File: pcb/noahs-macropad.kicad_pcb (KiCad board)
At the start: 2 copper layers, 99 x 39 mm, 17 parts, among them U1 MOUDLE-SEEEDUINO-XIAO

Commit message: moved things around, to make it look less like an offcentered brick
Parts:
- added D10: LED_SK6812MINI, ScottoKeebs_Components:LED_SK6812MINI, F.Cu at (75.0, 121.4)
- added D11: LED_SK6812MINI, ScottoKeebs_Components:LED_SK6812MINI, F.Cu at (75.0, 125.5)
- added D12: LED_SK6812MINI, ScottoKeebs_Components:LED_SK6812MINI, F.Cu at (75.0, 129.6)
- added D13: LED_SK6812MINI, ScottoKeebs_Components:LED_SK6812MINI, F.Cu at (75.0, 133.8)
- added D14: LED_SK6812MINI, ScottoKeebs_Components:LED_SK6812MINI, F.Cu at (75.0, 137.9)
- added D15: LED_SK6812MINI, ScottoKeebs_Components:LED_SK6812MINI, F.Cu at (75.0, 142.0)
- added D16: LED_SK6812MINI, ScottoKeebs_Components:LED_SK6812MINI, F.Cu at (74.9, 146.2)
- added D9: LED_SK6812MINI, ScottoKeebs_Components:LED_SK6812MINI, F.Cu at (75.0, 117.3)
- added J1: OLED_128x32, ScottoKeebs_Components:OLED_128x32, F.Cu at (76.9, 41.3)
- moved U1 102.8 mm to (122.4, 52.2)
- moved S1 52.6 mm to (86.5, 57.9)
- moved S5 52.6 mm to (86.5, 76.9)
- moved S2 52.6 mm to (105.5, 57.9)
- moved S3 52.6 mm to (124.5, 57.9)
- moved S6 52.6 mm to (105.5, 76.9)
- moved S7 52.6 mm to (124.5, 76.9)
- moved S4 52.6 mm to (143.5, 57.9)
- moved S8 52.6 mm to (143.5, 76.9)
- moved D4 46.0 mm to (80.4, 127.6), turned to 0 degrees
- moved D8 44.8 mm to (80.4, 141.8), turned to 0 degrees
- moved D3 28.3 mm to (80.4, 124.1), turned to 0 degrees
- moved D7 26.9 mm to (80.4, 138.3), turned to 0 degrees
- moved D5 11.7 mm to (80.4, 131.2), turned to 0 degrees
- moved D1 11.7 mm to (80.4, 117.0), turned to 0 degrees
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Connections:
- U1 pad 1: unconnected-(U1-PA02_A0_D0-Pad1) -> LED0_DIN
- U1 pad 12: unconnected-(U1-3V3-Pad12) -> OLED_VCC
- U1 pad 13: GND -> LED_GND
- U1 pad 14: unconnected-(U1-5V-Pad14) -> 5V
- U1 pad 3: unconnected-(U1-PA10_A2_D2-Pad3) -> Row 0
- U1 pad 4: unconnected-(U1-PA11_A3_D3-Pad4) -> Row 1
- U1 pad 5: Row 0 -> OLED_SDA
- U1 pad 6: Row 1 -> OLED_SCL
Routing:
- net Row 1: track 100.5 -> 0.00 mm
- net Row 0: track 94.6 -> 0.00 mm
- net Col 3: track 94.5 -> 0.00 mm
- net Col 2: track 75.9 -> 0.00 mm
- net Col 1: track 58.1 -> 0.00 mm, vias 2 -> 0
- net Col 0: track 51.0 -> 0.00 mm
- net Net-(D3-A): track 13.4 -> 0.00 mm
- net Net-(D2-A): track 13.4 -> 0.00 mm
- net Net-(D7-A): track 13.4 -> 0.00 mm
- net Net-(D6-A): track 13.4 -> 0.00 mm
- net Net-(D5-A): track 13.4 -> 0.00 mm
- net Net-(D1-A): track 13.3 -> 0.00 mm
- net Net-(D4-A): track 11.9 -> 0.00 mm
- net Net-(D8-A): track 11.9 -> 0.00 mm
- removed copper zone on B.Cu, net (none)
- removed copper zone on F.Cu, net (none)
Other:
- board size 99 x 39 mm -> 3.4 x 3 mm
- board text removed: "18/02/26"
- board text removed: "Made with <3 by Noah Sheppard"

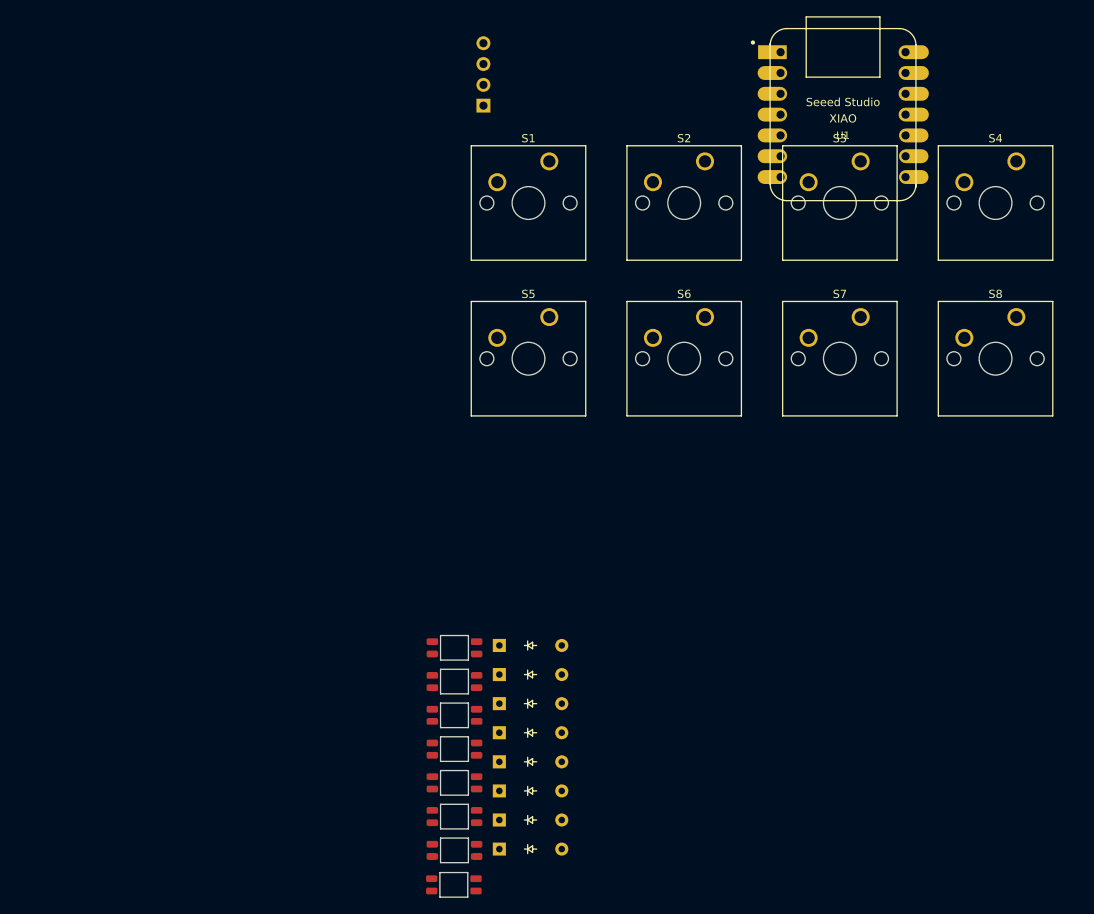
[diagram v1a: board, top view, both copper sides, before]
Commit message: finished PCB - my dumbass had the SEEED Xiao mounted to the front of the PCB in which it would be "below" a switch (wouldn't be phsycially possible) - put it on the bottom you say? With the way I did wiring, that would put your 5V pin from the Xiao into GND and vice versa - kaboom? Cheeky rewire later and we should be good as gold. Should be...
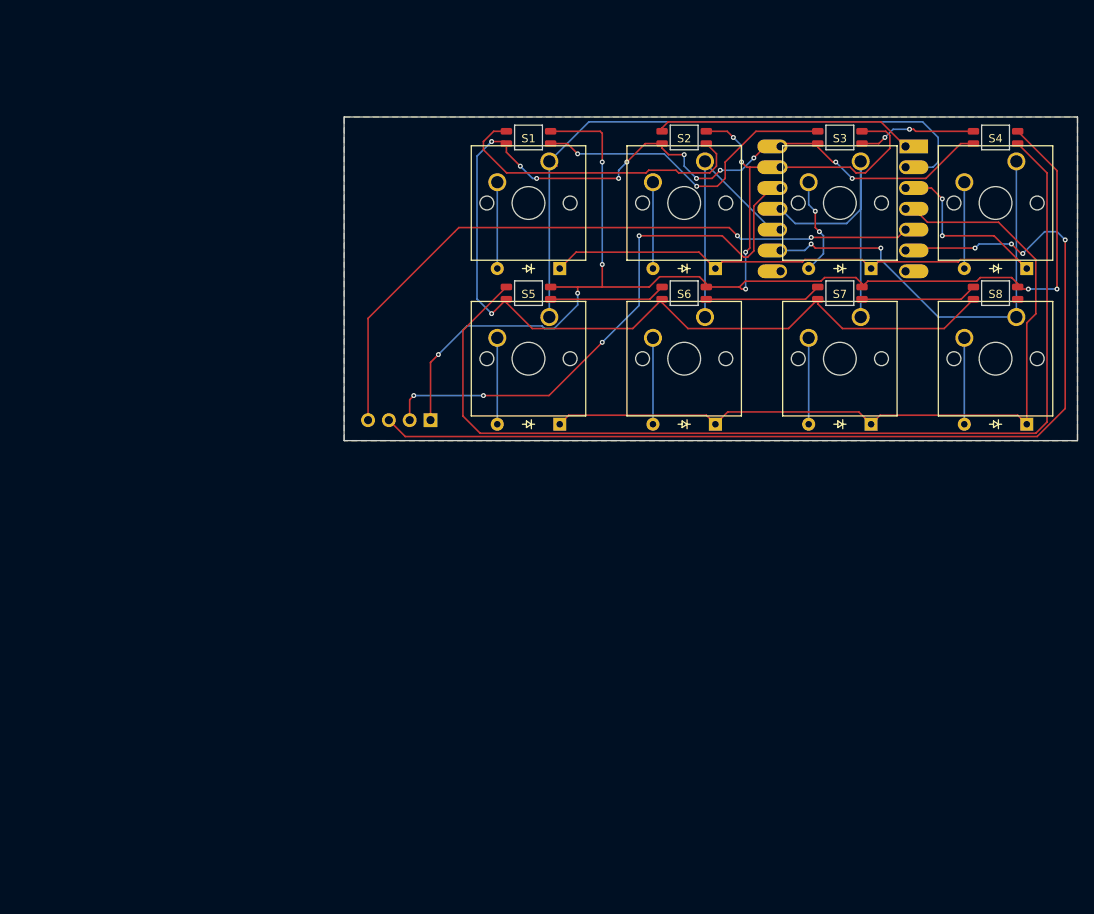
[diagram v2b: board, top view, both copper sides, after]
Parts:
- U1: moved to B.Cu
- moved D12 99.7 mm to (141.0, 55.0)
- moved D16 97.9 mm to (141.0, 74.0)
- moved D4 85.7 mm to (144.8, 71.0), turned to 180 degrees
- moved D11 84.8 mm to (122.0, 55.0)
- moved D15 82.7 mm to (122.0, 74.0)
- moved D8 82.7 mm to (144.8, 90.0), turned to 180 degrees
- moved D10 72.1 mm to (103.0, 55.0)
- moved D3 69.8 mm to (125.8, 71.0), turned to 180 degrees
- moved D14 69.8 mm to (103.0, 74.0)
- moved D7 66.3 mm to (125.8, 90.0), turned to 180 degrees
- moved D9 62.9 mm to (84.0, 55.0)
- moved D13 60.4 mm to (84.0, 74.0)
- moved D2 56.1 mm to (106.8, 71.0), turned to 180 degrees
- moved D6 51.9 mm to (106.8, 90.0), turned to 180 degrees
- moved J1 51.9 mm to (62.2, 91.1), turned to 90 degrees
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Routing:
- net LED_GND: track 0.00 -> 190.8 mm, vias 0 -> 10
- net 5V: track 0.00 -> 163.7 mm, vias 0 -> 12
- net OLED_SCL: track 0.00 -> 127.2 mm, vias 0 -> 4
- net Net-(D12-DOUT): track 0.00 -> 126.1 mm
- net Row 1: track 0.00 -> 99.1 mm
- net OLED_SDA: track 0.00 -> 83.7 mm, vias 0 -> 2
- net Row 0: track 0.00 -> 82.0 mm, vias 0 -> 2
- net Col 0: track 0.00 -> 77.7 mm
- net OLED_VCC: track 0.00 -> 68.8 mm, vias 0 -> 4
- net Col 3: track 0.00 -> 52.6 mm, vias 0 -> 2
- net Net-(D11-DIN): track 0.00 -> 38.7 mm, vias 0 -> 2
- net Net-(D10-DOUT): track 0.00 -> 37.8 mm
- net Col 2: track 0.00 -> 36.1 mm
- net Col 1: track 0.00 -> 31.8 mm
- net LED0_DIN: track 0.00 -> 31.7 mm
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- added copper zone on B.Cu, net (none)
- added copper zone on F.Cu, net (none)
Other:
- board size 3.4 x 3 mm -> 89.5 x 39.5 mm
